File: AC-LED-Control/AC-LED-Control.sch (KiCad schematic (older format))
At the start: 14 parts, among them P1 CONN_01X02, P2 CONN_01X02, SW1 SW_PUSH, U1 STM32F030F4P6, U2 74HC595, U3 74HC595

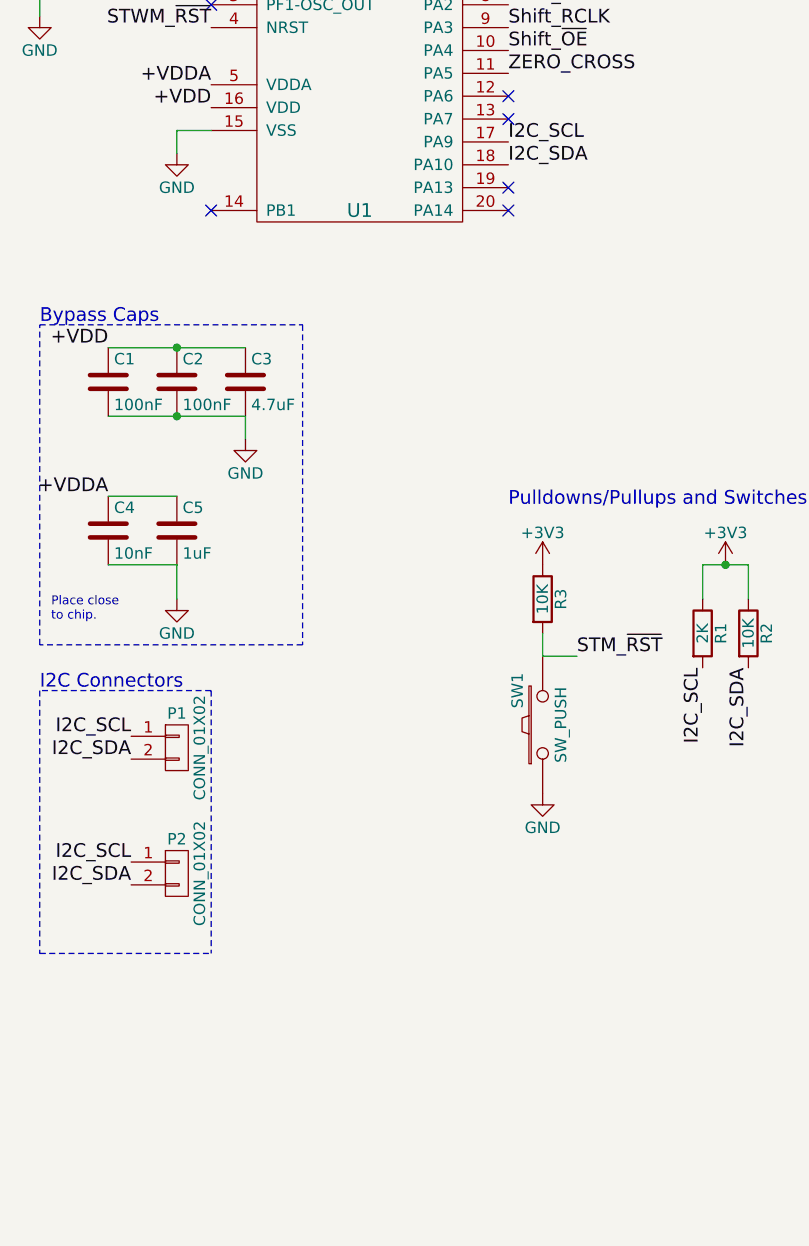
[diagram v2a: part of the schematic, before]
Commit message: Added SWD
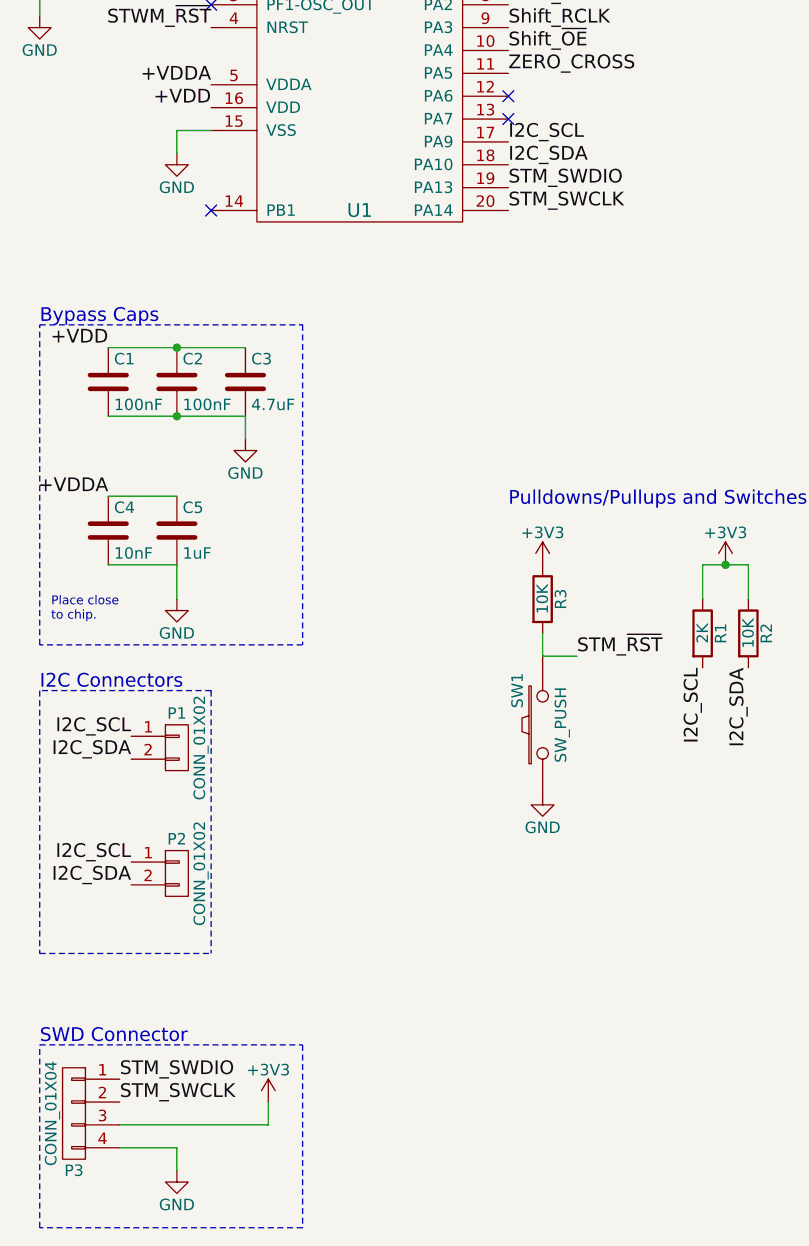
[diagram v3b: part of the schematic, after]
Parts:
- added P3: CONN_01X04, symbol CONN_01X04
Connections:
- net +3V3: now also P3.3 (P3)
- net GND: now also P3.4 (P4)
- net STM_SWDIO: now reaches U1.19 (PA13)
- net STM_SWDIO: now also P3.1 (P1)
- net STM_SWCLK: now reaches U1.20 (PA14)
- net STM_SWCLK: now also P3.2 (P2)
- no-connect marks 8 -> 6
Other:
- note added: "SWD Connector\n"
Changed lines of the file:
@@
 $EndComp
 $Comp
-L +3V3 #PWR01
+L +3V3 #PWR9
 U 1 1 5B45401C
 P 3800 3650
-F 0 "#PWR01" H 3800 3500 50  0001 C CNN
+F 0 "#PWR9" H 3800 3500 50  0001 C CNN
 F 1 "+3V3" H 3800 3790 50  0000 C CNN
 F 2 "" H 3800 3650 50  0000 C CNN
@@
 	1400 1750 1400 1850
 $Comp
-L GND #PWR02
+L GND #PWR4
 U 1 1 5B454DB5
 P 1400 1850
-F 0 "#PWR02" H 1400 1600 50  0001 C CNN
+F 0 "#PWR4" H 1400 1600 50  0001 C CNN
 F 1 "GND" H 1400 1700 50  0000 C CNN
 F 2 "" H 1400 1850 50  0000 C CNN
@@
 $EndComp
 $Comp
-L GND #PWR03
+L GND #PWR7
 U 1 1 5B454DF7
 P 1700 3100
-F 0 "#PWR03" H 1700 2850 50  0001 C CNN
+F 0 "#PWR7" H 1700 2850 50  0001 C CNN
 F 1 "GND" H 1700 2950 50  0000 C CNN
 F 2 "" H 1700 3100 50  0000 C CNN
@@
 $EndComp
 $Comp
-L GND #PWR04
+L GND #PWR10
 U 1 1 5B454F8F
 P 1400 3800
-F 0 "#PWR04" H 1400 3550 50  0001 C CNN
+F 0 "#PWR10" H 1400 3550 50  0001 C CNN
 F 1 "GND" H 1400 3650 50  0000 C CNN
 F 2 "" H 1400 3800 50  0000 C CNN
@@
 	8300 1400 8300 1250
 $Comp
-L +3V3 #PWR05
+L +3V3 #PWR3
 U 1 1 5B455E79
 P 8300 1250
-F 0 "#PWR05" H 8300 1100 50  0001 C CNN
+F 0 "#PWR3" H 8300 1100 50  0001 C CNN
 F 1 "+3V3" H 8300 1390 50  0000 C CNN
 F 2 "" H 8300 1250 50  0000 C CNN
@@
 	8300 2500 8300 2650
 $Comp
-L GND #PWR06
+L GND #PWR6
 U 1 1 5B455F67
 P 8300 2650
-F 0 "#PWR06" H 8300 2400 50  0001 C CNN
+F 0 "#PWR6" H 8300 2400 50  0001 C CNN
 F 1 "GND" H 8300 2500 50  0000 C CNN
 F 2 "" H 8300 2650 50  0000 C CNN
@@
 	5700 1400 5700 1250
 $Comp
-L +3V3 #PWR07
+L +3V3 #PWR2
 U 1 1 5B456028
 P 5700 1250
-F 0 "#PWR07" H 5700 1100 50  0001 C CNN
+F 0 "#PWR2" H 5700 1100 50  0001 C CNN
 F 1 "+3V3" H 5700 1390 50  0000 C CNN
 F 2 "" H 5700 1250 50  0000 C CNN
@@
 	5700 2500 5700 2650
 $Comp
-L GND #PWR08
+L GND #PWR5
 U 1 1 5B4560F7
 P 5700 2650
-F 0 "#PWR08" H 5700 2400 50  0001 C CNN
+F 0 "#PWR5" H 5700 2400 50  0001 C CNN
 F 1 "GND" H 5700 2500 50  0000 C CNN
 F 2 "" H 5700 2650 50  0000 C CNN
@@
 NoConn ~ 2850 1600
 NoConn ~ 2850 1700
-NoConn ~ 2850 2000
-NoConn ~ 2850 2100
 NoConn ~ 1550 1100
 NoConn ~ 1550 1200
@@
 	3000 4050 3000 3950
 $Comp
-L +3V3 #PWR09
+L +3V3 #PWR8
 U 1 1 5B4571F5
 P 3000 3650
-F 0 "#PWR09" H 3000 3500 50  0001 C CNN
+F 0 "#PWR8" H 3000 3500 50  0001 C CNN
 F 1 "+3V3" H 3000 3790 50  0000 C CNN
 F 2 "" H 3000 3650 50  0000 C CNN
@@
 $EndComp
 $Comp
-L GND #PWR010
+L GND #PWR11
 U 1 1 5B4575F8
 P 3000 4650
-F 0 "#PWR010" H 3000 4400 50  0001 C CNN
+F 0 "#PWR11" H 3000 4400 50  0001 C CNN
 F 1 "GND" H 3000 4500 50  0000 C CNN
 F 2 "" H 3000 4650 50  0000 C CNN
@@
 	800  1000 800  1250
 $Comp
-L GND #PWR011
+L GND #PWR1
 U 1 1 5B45876A
 P 800 1250
-F 0 "#PWR011" H 800 1000 50  0001 C CNN
+F 0 "#PWR1" H 800 1000 50  0001 C CNN
 F 1 "GND" H 800 1100 50  0000 C CNN
 F 2 "" H 800 1250 50  0000 C CNN
@@
 	1    0    0    -1
 $EndComp
+Text Label 2850 2000 0    60   ~ 0
+STM_SWDIO
+Text Label 2850 2100 0    60   ~ 0
+STM_SWCLK
+Text Label 1150 5900 0    60   ~ 0
+STM_SWDIO
+Text Label 1150 6000 0    60   ~ 0
+STM_SWCLK
+Text Notes 800  5750 0    60   ~ 0
+SWD Connector\n
+$Comp
+L CONN_01X04 P3
+U 1 1 5B459213
+P 950 6050
+F 0 "P3" H 950 5800 50  0000 C CNN
+F 1 "CONN_01X04" V 1050 6050 50  0000 C CNN
+F 2 "" H 950 6050 50  0000 C CNN
+F 3 "" H 950 6050 50  0000 C CNN
+	1    950  6050
+	-1   0    0    -1
+$EndComp
+Wire Wire Line
+	1150 6100 1800 6100
+Wire Wire Line
+	1800 6100 1800 6000
+$Comp
+L +3V3 #PWR12
+U 1 1 5B4593A7
+P 1800 6000
+F 0 "#PWR12" H 1800 5850 50  0001 C CNN
+F 1 "+3V3" H 1800 6140 50  0000 C CNN
+F 2 "" H 1800 6000 50  0000 C CNN
+F 3 "" H 1800 6000 50  0000 C CNN
+	1    1800 6000
+	1    0    0    -1
+$EndComp
+Wire Wire Line
+	1150 6200 1400 6200
+Wire Wire Line
+	1400 6200 1400 6300
+$Comp
+L GND #PWR13
+U 1 1 5B459412
+P 1400 6300
+F 0 "#PWR13" H 1400 6050 50  0001 C CNN
+F 1 "GND" H 1400 6150 50  0000 C CNN
+F 2 "" H 1400 6300 50  0000 C CNN
+F 3 "" H 1400 6300 50  0000 C CNN
+	1    1400 6300
+	1    0    0    -1
+$EndComp
+Wire Notes Line
+	800  5750 1950 5750
+Wire Notes Line
+	1950 5750 1950 6550
+Wire Notes Line
+	1950 6550 800  6550
+Wire Notes Line
+	800  6550 800  5750
 $EndSCHEMATC

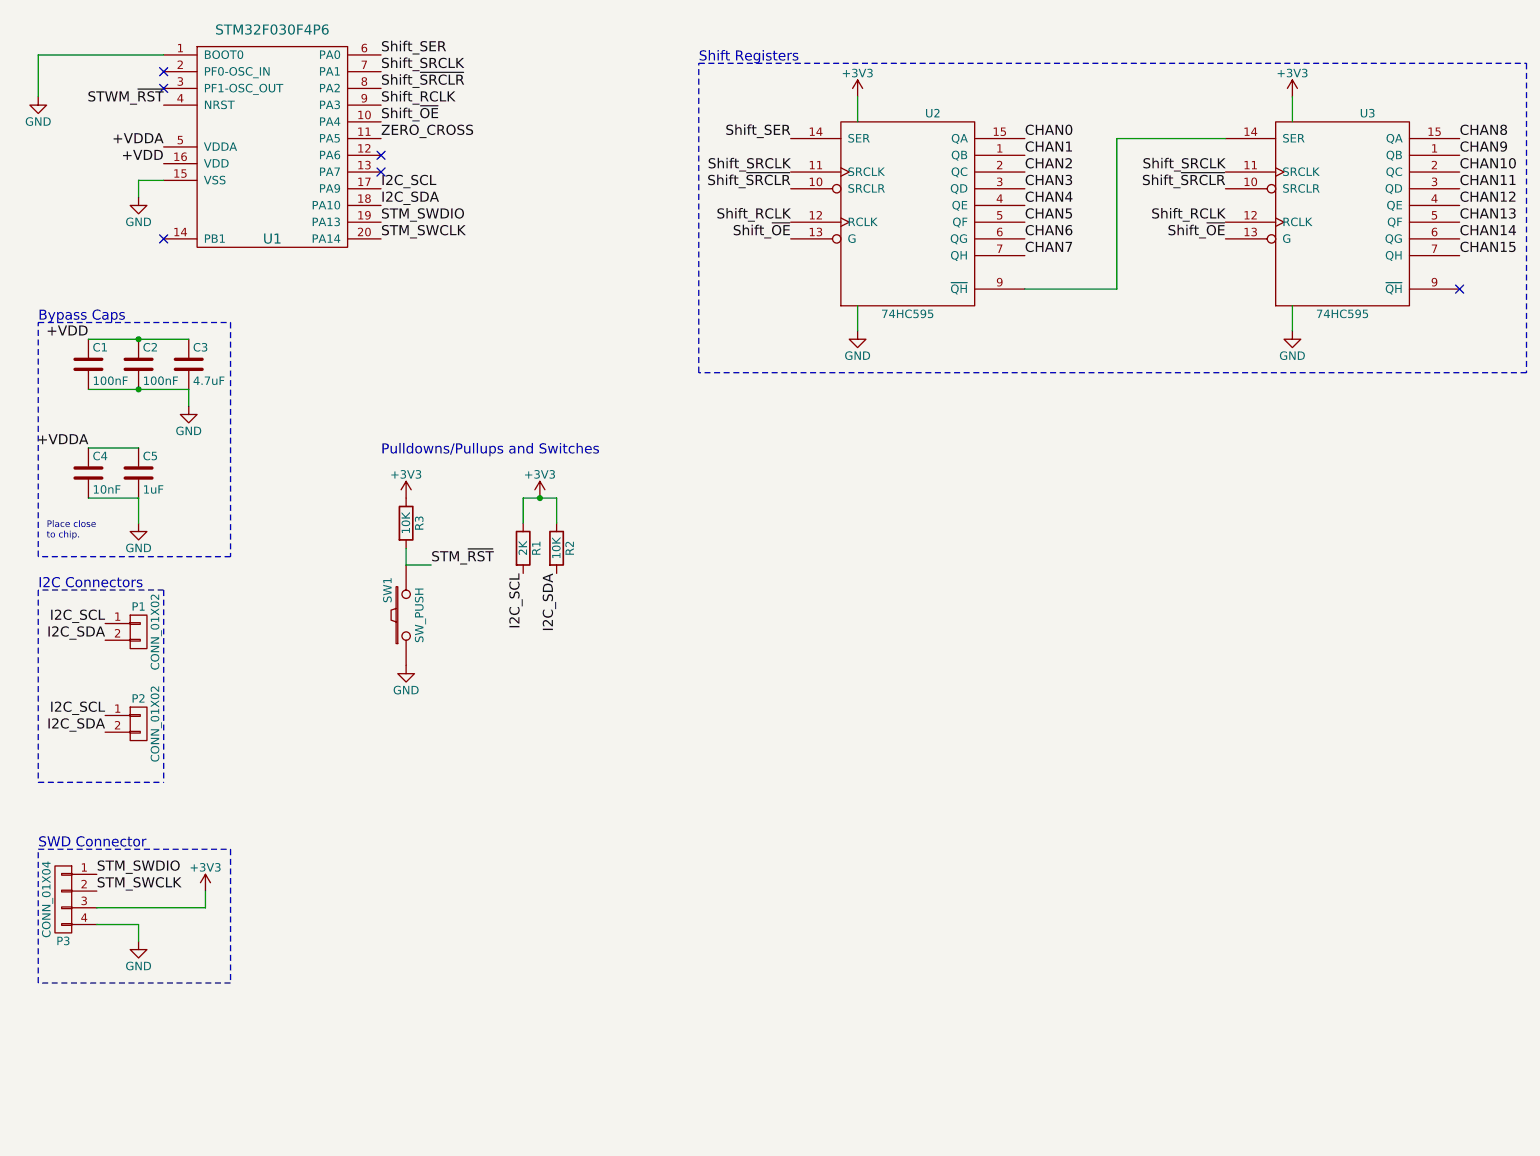
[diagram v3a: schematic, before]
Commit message: Added zero cross detector
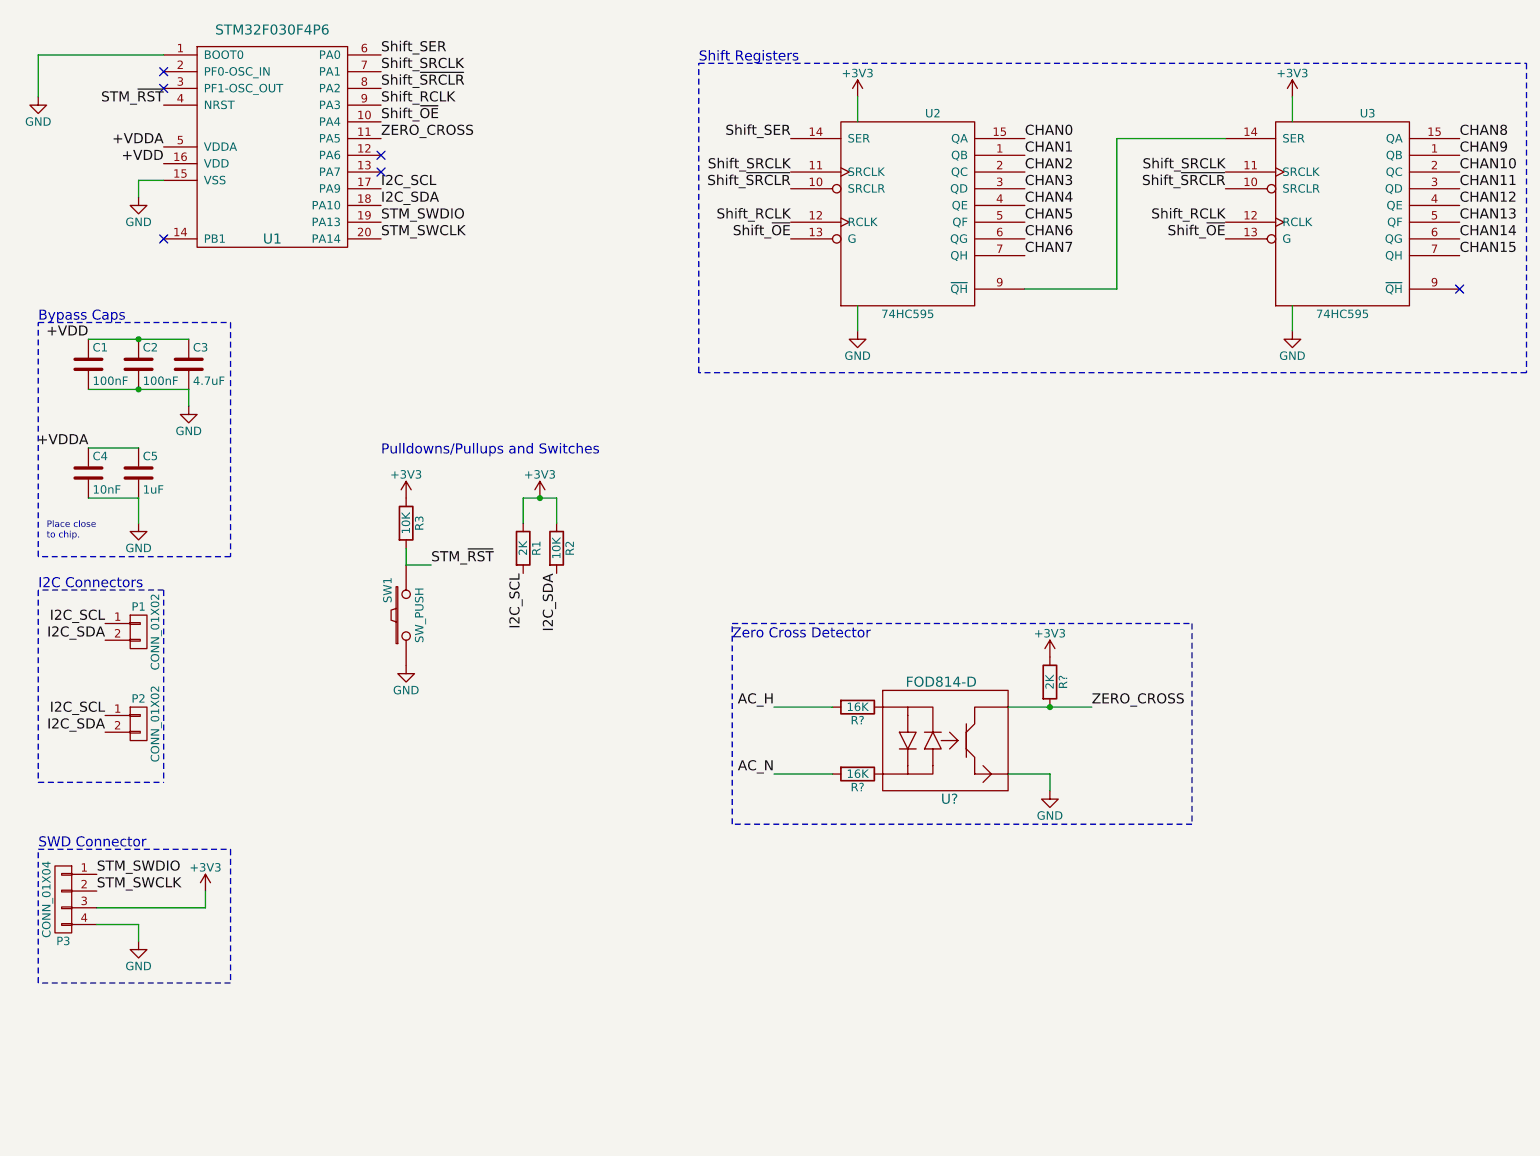
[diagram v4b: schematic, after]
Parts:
- added R? (x2): 16K, symbol R
- added R?: 2K, symbol R
- added U?: FOD814-D, symbol FOD814-D
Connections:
- net STWM_~RST is gone; now on net STM_~RST: U1.4 (NRST)
- net +3V3: now also R?.1
- net GND: now also U?.3 (EMITTER)
- net ZERO_CROSS: now also R?.2, U?.4 (COLLECTOR)
- new net: R?.1, U?.1 (AC)
- new net: R?.1, U?.2 (AC)
- new net AC_H: R?.2
- new net AC_N: R?.2
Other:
- note added: "Zero Cross Detector"
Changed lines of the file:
@@
 LIBS:symbols
 LIBS:stm32f030f4p6
+LIBS:fod814-d
 LIBS:AC-LED-Control-cache
 EELAYER 25 0
@@
 NoConn ~ 1550 1200
 Text Label 1550 1300 2    60   ~ 0
-STWM_~RST
+STM_~RST
 Text Label 3150 4050 0    60   ~ 0
 STM_~RST
@@
 Wire Notes Line
 	800  6550 800  5750
+Text Notes 4950 4500 0    60   ~ 0
+Zero Cross Detector
+$Comp
+L R R?
+U 1 1 5B46350A
+P 5700 4900
+F 0 "R?" V 5780 4900 50  0000 C CNN
+F 1 "16K" V 5700 4900 50  0000 C CNN
+F 2 "" V 5630 4900 50  0000 C CNN
+F 3 "" H 5700 4900 50  0000 C CNN
+	1    5700 4900
+	0    1    1    0
+$EndComp
+$Comp
+L FOD814-D U?
+U 1 1 5B46379C
+P 6250 5200
+F 0 "U?" H 6250 4950 60  0000 C CNN
+F 1 "FOD814-D" H 6200 5650 60  0000 C CNN
+F 2 "" H 6200 5200 60  0000 C CNN
+F 3 "" H 6200 5200 60  0000 C CNN
+	1    6250 5200
+	1    0    0    -1
+$EndComp
+$Comp
+L R R?
+U 1 1 5B463817
+P 5700 5300
+F 0 "R?" V 5780 5300 50  0000 C CNN
+F 1 "16K" V 5700 5300 50  0000 C CNN
+F 2 "" V 5630 5300 50  0000 C CNN
+F 3 "" H 5700 5300 50  0000 C CNN
+	1    5700 5300
+	0    1    1    0
+$EndComp
+Wire Wire Line
+	5550 4900 5200 4900
+Wire Wire Line
+	5550 5300 5200 5300
+Text Label 5200 4900 2    60   ~ 0
+AC_H
+Text Label 5200 5300 2    60   ~ 0
+AC_N
+Wire Wire Line
+	6600 4900 7100 4900
+$Comp
+L R R?
+U 1 1 5B463CCD
+P 6850 4750
+F 0 "R?" V 6930 4750 50  0000 C CNN
+F 1 "2K" V 6850 4750 50  0000 C CNN
+F 2 "" V 6780 4750 50  0000 C CNN
+F 3 "" H 6850 4750 50  0000 C CNN
+	1    6850 4750
+	1    0    0    -1
+$EndComp
+$Comp
+L +3V3 #PWR?
+U 1 1 5B463D3E
+P 6850 4600
+F 0 "#PWR?" H 6850 4450 50  0001 C CNN
+F 1 "+3V3" H 6850 4740 50  0000 C CNN
+F 2 "" H 6850 4600 50  0000 C CNN
+F 3 "" H 6850 4600 50  0000 C CNN
+	1    6850 4600
+	1    0    0    -1
+$EndComp
+Connection ~ 6850 4900
+Text Label 7100 4900 0    60   ~ 0
+ZERO_CROSS
+Wire Wire Line
+	6600 5300 6850 5300
+Wire Wire Line
+	6850 5300 6850 5400
+$Comp
+L GND #PWR?
+U 1 1 5B464157
+P 6850 5400
+F 0 "#PWR?" H 6850 5150 50  0001 C CNN
+F 1 "GND" H 6850 5250 50  0000 C CNN
+F 2 "" H 6850 5400 50  0000 C CNN
+F 3 "" H 6850 5400 50  0000 C CNN
+	1    6850 5400
+	1    0    0    -1
+$EndComp
+Wire Notes Line
+	4950 4400 7700 4400
+Wire Notes Line
+	7700 4400 7700 5600
+Wire Notes Line
+	7700 5600 4950 5600
+Wire Notes Line
+	4950 5600 4950 4400
 $EndSCHEMATC
